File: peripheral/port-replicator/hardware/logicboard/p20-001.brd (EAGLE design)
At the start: 72 x 72 mm, 64 parts, among them IC1 74LS07N, IC11 74LS153D, IC12 LTC485S, IC13 LTC485S, IC2 4066N, J1 MKR, J11 Qwiic, J12 Qwiic, J13 Qwiic, J14 Qwiic, J2 GPIO, J3 Vout, J4 RLY, J5 SPI, J6 LED, K1 G5V1, T1 2SC1815, U1 DS18B20

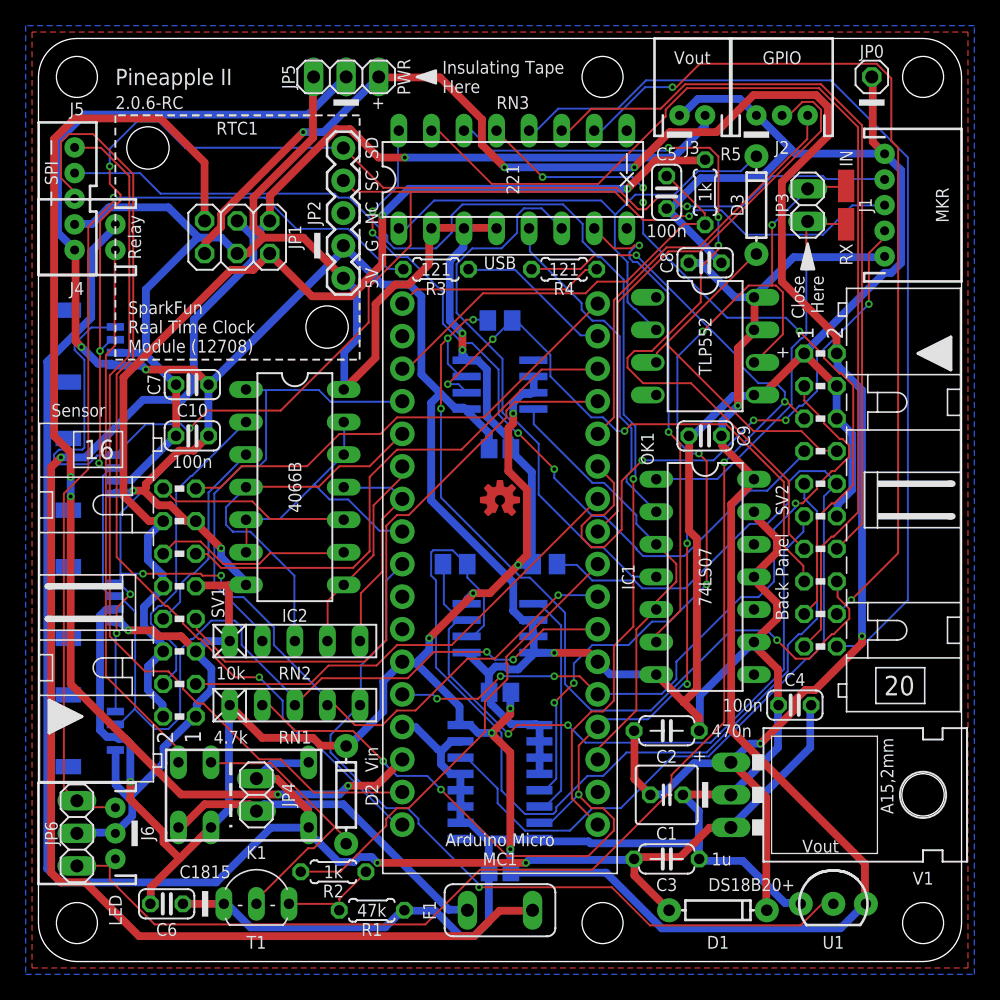
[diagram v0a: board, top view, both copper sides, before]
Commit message: Cleared unnecessary parts.
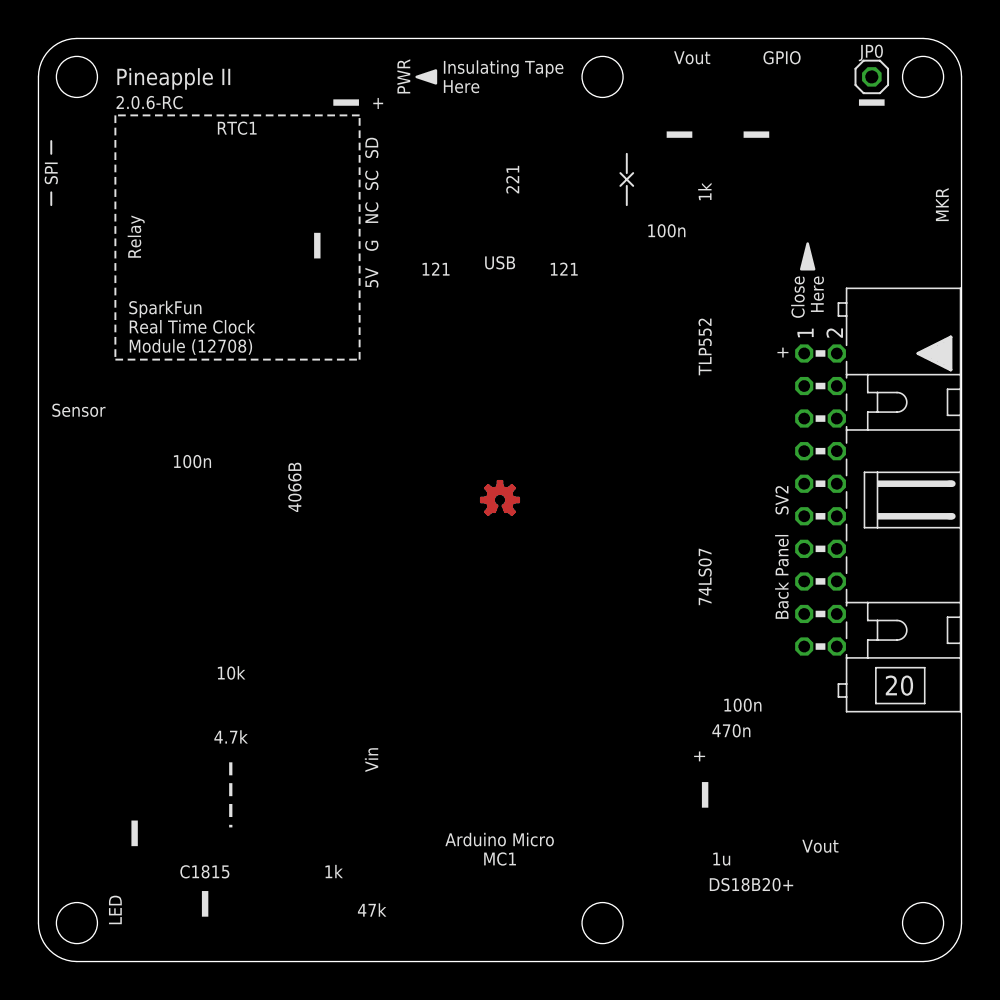
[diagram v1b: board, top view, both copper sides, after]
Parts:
- removed C1: 22u, rcl:C025-050X050
- removed C10, C4, C5: 100n, rcl:C025-024X044
- removed C11, C12, C13: 10n, rcl:C2012
- removed C2: 470n, rcl:C050-024X044
- removed C3: 1u, rcl:C050-024X044
- removed C6, C7, C8, C9: 10n, resistor:C025-024X044
- removed D1, D2, D3: (no value), SparkFun-DiscreteSemi:DIODE-1N4148
- removed F1: 1.8A, fuse:TE5
- removed H1, H2: STAND-OFF, SparkFun-Hardware:STAND-OFF
- removed IC1: 74LS07N, 74xx-us:DIL14
- removed IC11: 74LS153D, 74xx-us:SO16
- removed IC12, IC13: LTC485S, linear-technology:SOIC8
- removed IC2: 4066N, 40xx:DIL14
- removed IN, RX: (no value), wirepad:SMD1,27-2,54
- removed J1: MKR, SparkFun-Connectors:JST-5-PTH
- removed J11, J12, J13, J14: Qwiic, SparkFun-Connectors:1X04_1MM_RA
- removed J2: GPIO, SparkFun-Connectors:JST-3-PTH
- removed J3: Vout, SparkFun-Connectors:JST-2-PTH
- removed J4: RLY, SparkFun-Connectors:JST-2-PTH
- removed J5: SPI, SparkFun-Connectors:JST-5-PTH-VERT
- removed J6: LED, SparkFun-Connectors:JST-3-PTH
- removed JP1: PWRSEL, pinhead:2X03
- removed JP2: RTC, SparkFun-Connectors:1X05
- removed JP3: MPXJMP, pinhead:1X02
- removed JP4: RLYJMP, pinhead:1X02
- removed JP5: D5V, pinhead:1X03
- removed JP6: LED, pinhead:1X03
- removed K1: G5V1, relay:G5V1
- removed MC1: ARDUINOMICRO, adafruit:ARDUINOMICRO
- removed OK1: 6N137, optocoupler:DIL08
- removed R1: 47k, resistor:0204/5
- removed R11: 10k, rcl:M2012
- removed R12, R13: 120, rcl:M2012
- removed R2, R5: 1k, resistor:0204/5
- removed R3, R4: 120, resistor:0204/5
- removed RN1: 4.7k, resistor-net:RN-5
- removed RN2: 10k, resistor-net:RN-5
- removed RN3: 220, resistor-dil:DIL16
- removed SV1: (no value), con-ml:ML16L
- removed T1: 2SC1815, transistor:TO92-ECB
- removed U1: DS18B20, SparkFun-Sensors:TO-92-AMMO
- removed V1: 5V, v-reg:78XXL
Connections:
- removed net ANLG1: IC2.1, MC1.P$31, RN2.2
- removed net ANLG1R: IC2.2, SV1.4
- removed net ANLG2: IC2.4, MC1.P$30, RN2.3
- removed net ANLG2R: IC2.3, SV1.8
- removed net ANLG3: IC2.8, MC1.P$29, RN2.4
- removed net ANLG3R: IC2.9, SV1.12
- removed net ANLG4: IC2.11, MC1.P$28, RN2.5
- removed net ANLG4R: IC2.10, SV1.16
- removed net AREF: C5.1, MC1.P$32, R5.1
- removed net D7: J1.4, MC1.P$6
- removed net DTCT1: MC1.P$7, SV1.3
- removed net DTCT2: MC1.P$4, SV1.7
- removed net DTCT3: MC1.P$3, SV1.11
- removed net DTCT4: MC1.P$1, SV1.15
- removed net GATE: IC2.12, IC2.13, IC2.5, IC2.6, MC1.P$27
- removed net GPIO1: J2.2, MC1.P$8
- removed net GPIO2: J2.3, MC1.P$5
- removed net LED0: MC1.P$34, R4.2
- removed net LED1: MC1.P$2, R3.2
- removed net LED1A: J6.3, JP6.3, R3.1
- removed net MIDIINSND: D3.C, OK1.2, RN3.1
- removed net MIN: IC11.5, IN.1, JP3.2, OK1.6
- removed net MISO: J5.5, MC1.P$19
- removed net MO1: IC1.4, RN3.6
- removed net MO2: IC1.6, RN3.7
- removed net MOSI: J5.4, MC1.P$17
- removed net MRX: IC11.6, IC12.1
- removed net MT: IC1.2, RN3.5
- removed net RLY: MC1.P$9, R2.2
- removed net RLYDRV: R1.2, R2.1, T1.B
- removed net RLYOUT: J4.1, K1.10
- removed net RLYSNK: D2.A, K1.9, T1.C
- removed net RX: IC1.1, IC11.7, JP3.1, MC1.P$14, RN1.2, RX.1
- removed net SCK: J5.3, MC1.P$18
- removed net SCL: J1.3, J11.4, J12.4, J13.4, J14.4, JP2.4, MC1.P$10, RN1.4
- removed net SDA: J1.2, J11.3, J12.3, J13.3, J14.3, JP2.5, MC1.P$11, RN1.3
- removed net THS: MC1.P$26, RN1.5, U1.2
- removed net TX: IC1.3, IC1.5, IC13.4, MC1.P$15
- removed net VCC: C10.1, C11.1, C12.1, C13.1, C6.1, C7.1, C8.1, C9.1, D2.C, IC1.14, IC11.16, IC12.8, IC13.2, IC13.3, IC13.8, IC2.14, J1.5, J11.2, J12.2, J13.2, J14.2, J5.2, JP1.3, JP2.1, JP5.1, K1.2, MC1.P$23, OK1.7, OK1.8, R11.2, RN1.1, RN3.2, RN3.3, RN3.4, U1.3
- removed net VCC/2: JP1.5, R5.2, SV1.10, SV1.14, SV1.2, SV1.6
- removed net VDD: MC1.P$33
- removed net VIN: JP1.2, MC1.P$20
- removed net VOUT: F1.2, J3.2, JP1.4, JP1.6
- removed net VOUTRAW: C3.1, C4.1, D1.A, J4.2, JP4.2, K1.5, K1.6, V1.OUT
- removed net VOUTRAW2: F1.1, JP4.1, K1.1
- net GND: no longer C1.2, C10.2, C11.2, C12.2, C13.2, C2.2, C3.2, C4.2, C5.2, C6.2, C7.2, C8.2, C9.2, IC1.11, IC1.13, IC1.7, IC1.9, IC11.1, IC11.10, IC11.11, IC11.12, IC11.13, IC11.15, IC11.2, IC11.3, IC11.4, IC11.8, IC12.2, IC12.3, IC12.4, IC12.5, IC13.5, IC2.7, J1.1, J11.1, J12.1, J13.1, J14.1, J2.1, J3.1, J5.1, J6.2, JP2.2, JP5.2, JP6.2, MC1.P$12, MC1.P$21, OK1.5, R1.1, RN2.1, SV1.1, SV1.13, SV1.5, SV1.9, T1.E, U1.1, V1.GND
- net LED0A: no longer J6.1, JP6.1, R4.1
- net MIRETN: no longer D3.A, OK1.3
- net MISEND: no longer RN3.16
- net MO1RETN: no longer RN3.11
- net MO1SEND: no longer RN3.14
- net MO2RETN: no longer RN3.10
- net MO2SEND: no longer RN3.13
- net MRX+: no longer IC12.6, R12.1
- net MRX-: no longer IC12.7, R12.2
- net MRXDTCT: no longer IC11.14, R11.1
- net MTRETN: no longer RN3.12
- net MTSEND: no longer RN3.15
- net MTX+: no longer IC13.6, R13.1
- net MTX-: no longer IC13.7, R13.2
- net RST: no longer MC1.P$13, MC1.P$22
- net V+: no longer C1.1, C2.1, D1.C, JP1.1, JP5.3, V1.IN
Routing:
- net GND: track 445.7 -> 0.00 mm, vias 6 -> 0
- net VCC: track 346.0 -> 0.00 mm, vias 11 -> 0
- net SCL: track 175.5 -> 0.00 mm, vias 7 -> 0
- net SDA: track 167.7 -> 0.00 mm, vias 6 -> 0
- net V+: track 148.1 -> 0.00 mm, vias 5 -> 0
- net VOUT: track 143.9 -> 0.00 mm, vias 2 -> 0
- net VOUTRAW: track 139.1 -> 0.00 mm, vias 2 -> 0
- net LED0A: track 116.3 -> 0.00 mm, vias 3 -> 0
- net RX: track 102.9 -> 0.00 mm, vias 6 -> 0
- net MOSI: track 97.3 -> 0.00 mm, vias 1 -> 0
- net VIN: track 92.0 -> 0.00 mm, vias 4 -> 0
- net VCC/2: track 89.1 -> 0.00 mm, vias 2 -> 0
- net MTSEND: track 82.0 -> 0.00 mm
- net MRXDTCT: track 78.1 -> 0.00 mm
- net LED1A: track 77.2 -> 0.00 mm, vias 1 -> 0
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- removed copper zone on layer 1, net GND
- removed copper zone on layer 16, net GND
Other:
- board text removed: "74153"
- board text removed: "Arduino"
- board text removed: "Bottom View"
- board text removed: "D7"
- board text removed: "Direct 5V"
- board text removed: "Dual"
- board text removed: "Ext>V+"
- board text removed: "G1"
- board text removed: "G2"
- board text removed: "GND"
- board text removed: "LED0"
- board text removed: "LED1"
- board text removed: "LTC485"
- board text removed: "MI"
- board text removed: "MIDIIN"
- board text removed: "MO"
- board text removed: "Open JP1"
- board text removed: "PWRSEL"
- board text removed: "Qwiic/5V"
- board text removed: "RELAY"
- board text removed: "RLYJMP"
- board text removed: "RX"
- board text removed: "Regulator"
- board text removed: "SCK"
- board text removed: "SCL"
- board text removed: "SDA"
- board text removed: "TX"
- board text removed: "V+"
- board text removed: "Vcc"
- board text removed: "Vcc/2"
- board text removed: "Vin>MC"
- board text removed: "Vo"
- board text removed: "Vout<MC"

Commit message: Parts only. No connection.
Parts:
- added J0: (no value), con-jack:SPC4077
- added J1, J2, J3: DIN5, SparkFun-Connectors:DIN5-RA-PTH
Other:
- board text added: "MIDI Port Replicator 1.0.0-Alpha"
- board text removed: "+"
- board text removed: "100n"
- board text removed: "10k"
- board text removed: "121"
- board text removed: "1k"
- board text removed: "1u"
- board text removed: "2.0.6-RC"
- board text removed: "221"
- board text removed: "4.7k"
- board text removed: "4066B"
- board text removed: "470n"
- board text removed: "47k"
- board text removed: "5V"
- board text removed: "74LS07"
- board text removed: "Arduino Micro"
- board text removed: "C1815"
- board text removed: "Close Here"
- board text removed: "DS18B20+"
- board text removed: "G"
- board text removed: "GPIO"
- board text removed: "Insulating Tape Here"
- board text removed: "LED"
- board text removed: "MC1"
- board text removed: "MKR"
- board text removed: "NC"
- board text removed: "PWR"
- board text removed: "RTC1"
- board text removed: "Relay"
- board text removed: "SC"
- board text removed: "SD"
- board text removed: "SPI"
- board text removed: "Sensor"
- board text removed: "SparkFun Real Time Clock Module (12708)"
- board text removed: "TLP552"
- board text removed: "USB"
- board text removed: "Vin"
- board text removed: "Vout"
